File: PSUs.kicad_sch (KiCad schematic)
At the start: 57 parts, among them J6 Barrel_Jack, J7 AMP171826-4, Q1 DMP3013SFV-7, U3 AP64501SP-13, U4 AP64501SP-13, U8 AP62300WU-7

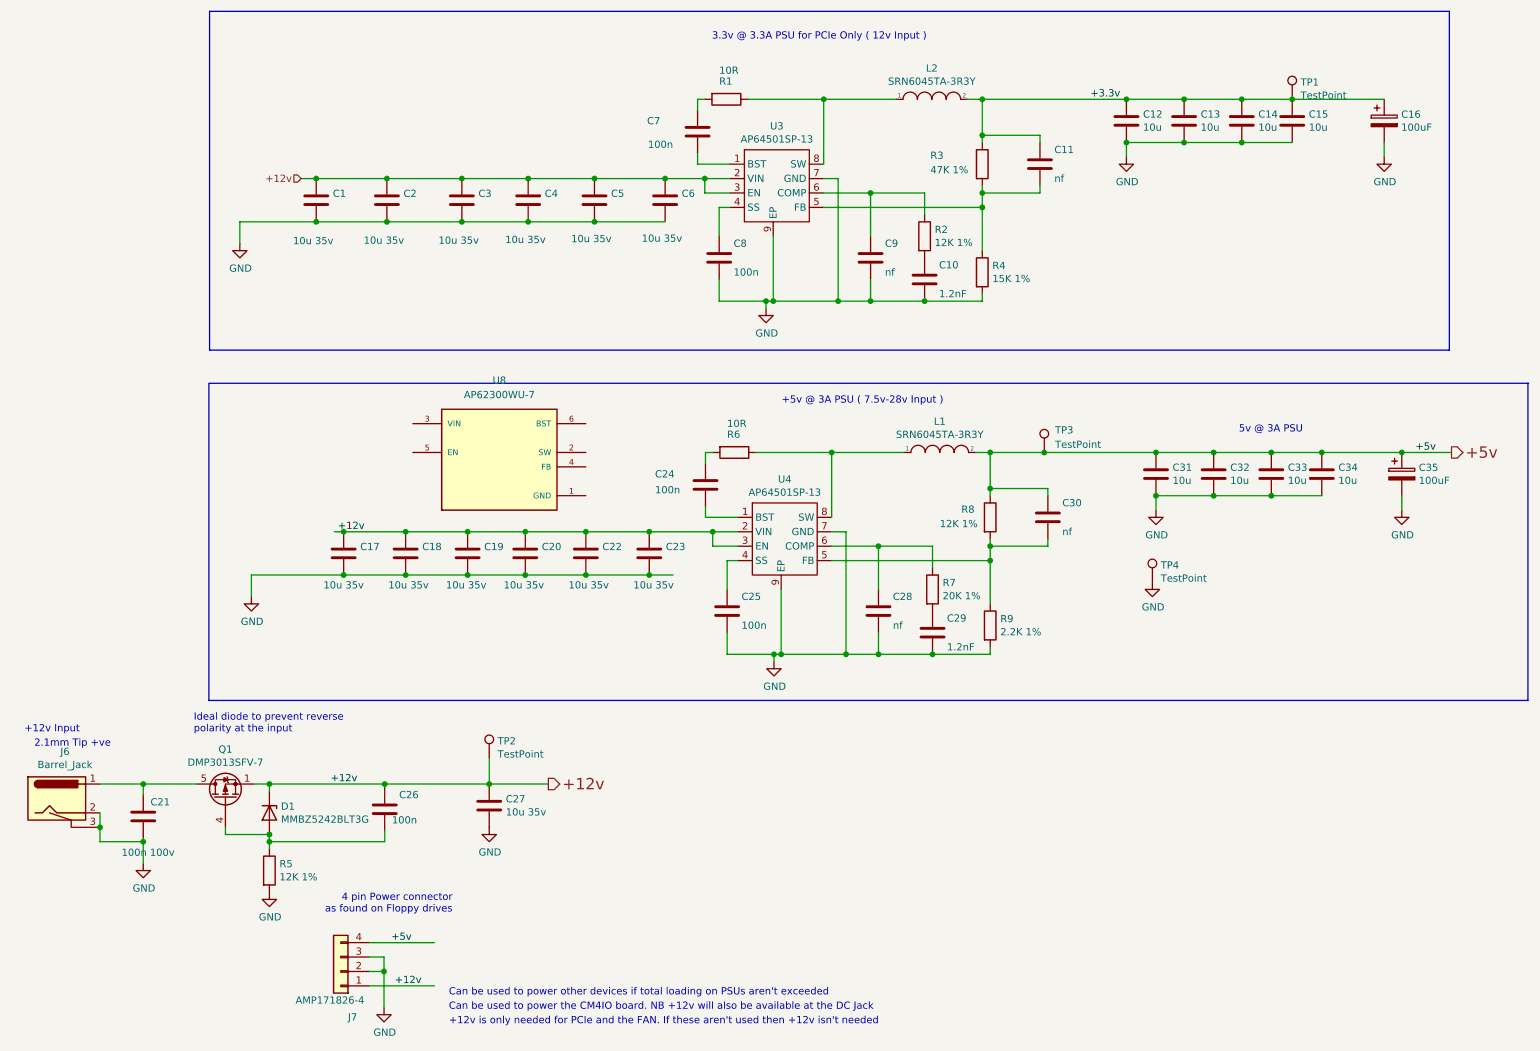
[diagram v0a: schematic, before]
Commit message: Added 3d-models, esd protection, cleaned up and made small start with pcb
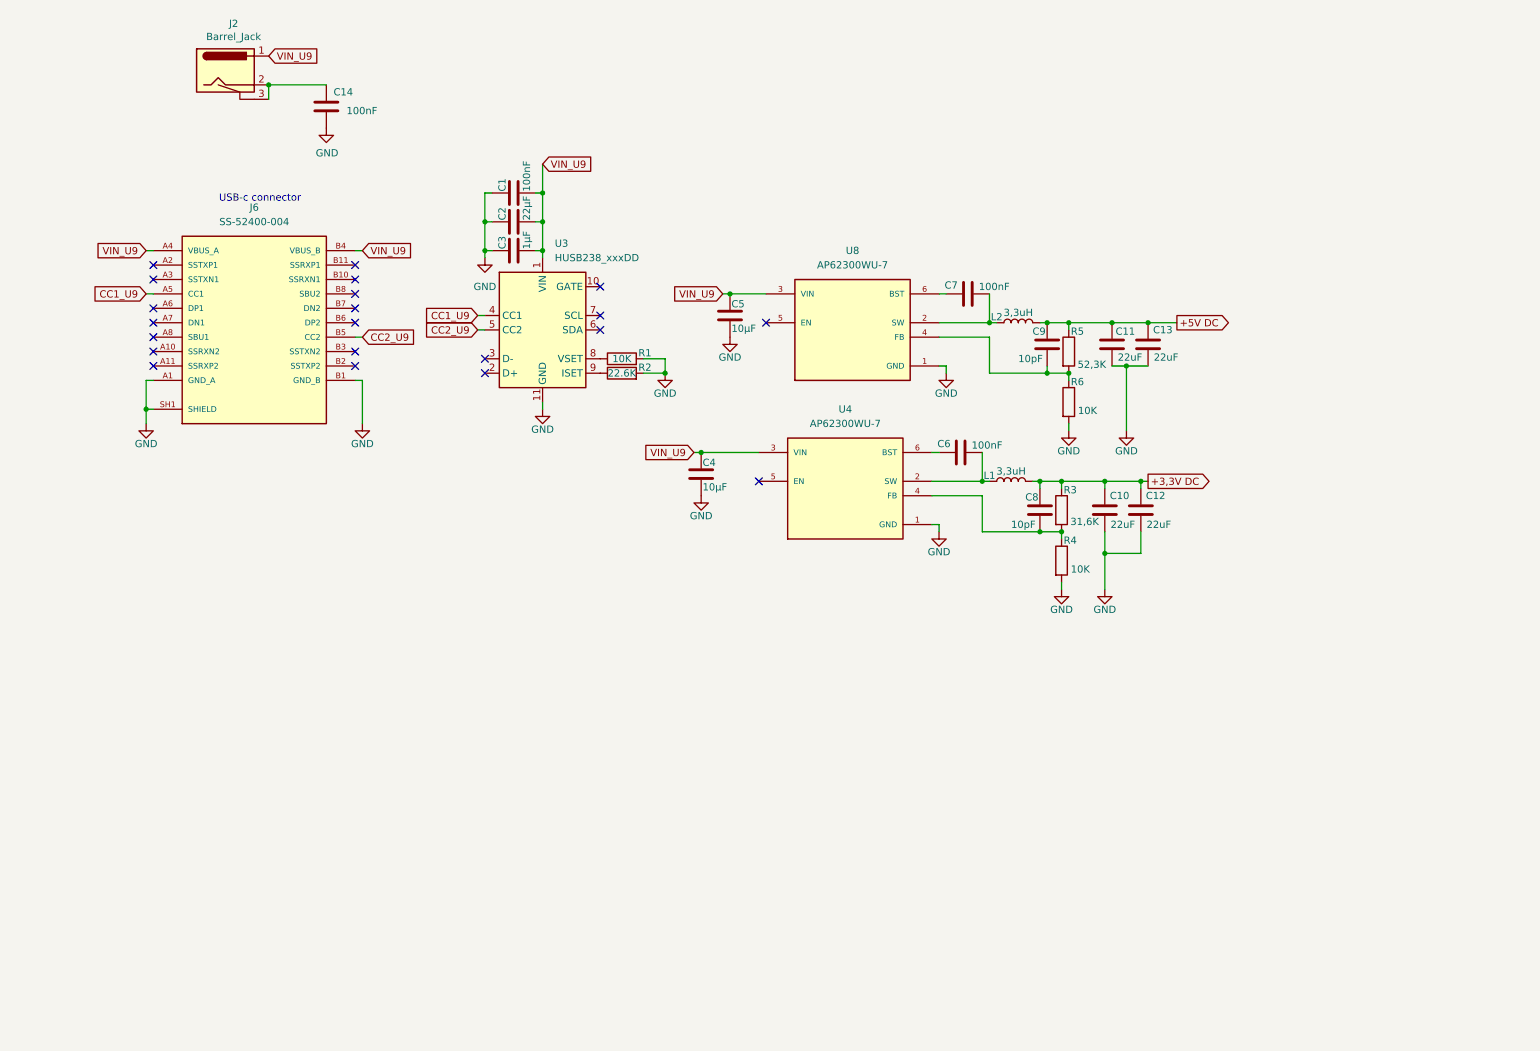
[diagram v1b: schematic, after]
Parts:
- removed C15, C31, C32, C33, C34: 10u, Capacitor_SMD:C_0805_2012Metric, symbol Device:C
- removed C16, C35: 100uF, Capacitor_Tantalum_SMD:CP_EIA-7343-31_Kemet-D, symbol Device:CP
- removed C17, C18, C19, C20, C22, C23, C27: 10u 35v, Capacitor_SMD:C_0805_2012Metric, symbol Device:C
- removed C21: 100n 100v, Capacitor_SMD:C_0402_1005Metric, symbol Device:C
- removed C24, C25, C26: 100n, Capacitor_SMD:C_0402_1005Metric, symbol Device:C
- removed C28, C30: nf, Capacitor_SMD:C_0402_1005Metric, symbol Device:C
- removed C29: 1.2nF, Capacitor_SMD:C_0402_1005Metric, symbol Device:C
- removed D1: MMBZ5242BLT3G, Diode_SMD:D_SOT-23_ANK, symbol Diode:BZX84Cxx
- removed J6: Barrel_Jack, CM4IO:BarrelJack_Horizontal, symbol CM4IO:Barrel_Jack
- removed J7: AMP171826-4, 171826-4:TE_171826-4, symbol Connector_Generic:Conn_01x04
- removed L1, L2: SRN6045TA-3R3Y, Inductor_SMD:L_Bourns_SRN6045TA, symbol pspice:INDUCTOR
- removed Q1: DMP3013SFV-7, Package_SON:Diodes_PowerDI3333-8, symbol Transistor_FET:DMP3013SFV
- removed R7: 20K 1%, Resistor_SMD:R_0402_1005Metric, symbol Device:R
- removed R8: 12K 1%, Resistor_SMD:R_0402_1005Metric, symbol Device:R
- removed R9: 2.2K 1%, Resistor_SMD:R_0402_1005Metric, symbol Device:R
- removed TP1, TP2, TP3, TP4: TestPoint, TestPoint:TestPoint_Pad_2.0x2.0mm, symbol Connector:TestPoint
- removed U3: AP64501SP-13, CM4IO:SOIC-8-1EP_3.9x4.9mm_P1.27mm_EP2.95x4.9mm_Mask2.71x3.4mm_ThermalVias, symbol CM4IO:AP64351
- removed U4: AP64501SP-13, Package_SO:SOIC-8-1EP_3.9x4.9mm_P1.27mm_EP2.95x4.9mm_Mask2.71x3.4mm_ThermalVias, symbol CM4IO:AP64351
- added J2: Barrel_Jack, CM4IO:BarrelJack_Horizontal, symbol CM4IO:Barrel_Jack
- added J6: SS-52400-004, SS-52400-004 (USB-c connector):STEWART_SS-52400-004 (USB-C), symbol SS-52400-004:SS-52400-004
- added L1, L2: 3,3uH, Inductor_SMD:L_0603_1608Metric, symbol Device:L
- added U3: HUSB238_xxxDD, Package_DFN_QFN:WDFN-10-1EP_3x3mm_P0.5mm_EP1.8x2.5mm, symbol Interface_USB:HUSB238_xxxDD
- added U4: AP62300WU-7, AP62300WU-7:SOT95P280X100-6N, symbol AP62300WU-7:AP62300WU-7
- C1, C6: value 10u 35v -> 100nF; footprint Capacitor_SMD:C_0805_2012Metric -> Capacitor_SMD:C_0603_1608Metric; Field4 Digikey -> (none); Field5 490-10505-1-ND -> (none); Field6 GRM21BC8YA106KE11L -> (none); Field7 Murata -> (none); Part Description 10uF 10% or 20% 35V Ceramic Capacitor X6S 0805 (2012 Metric) -> (none)
- C10: value 1.2nF -> 22uF; footprint Capacitor_SMD:C_0402_1005Metric -> Capacitor_SMD:C_0603_1608Metric; Field4 Digikey -> (none); Field5 490-16429-1-ND -> (none); Field6 GCM155R71H122KA37D -> (none); Field7 Murata -> (none); Part Description 1200pF 10% 10V Ceramic Capacitor X5R 0402 (1005 Metric) -> (none)
- C11: value nf -> 22uF; footprint Capacitor_SMD:C_0402_1005Metric -> Capacitor_SMD:C_0603_1608Metric; Field4 Digikey -> (none); Field5 490-17672-2-ND -> (none); Field6 GJM1555C1H270JB01D -> (none); Field7 Murata -> (none); Part Description 27pF 5% 50V Ceramic Capacitor C0G, NP0 0402 (1005 Metric) -> (none)
- C12, C13: value 10u -> 22uF; footprint Capacitor_SMD:C_0805_2012Metric -> Capacitor_SMD:C_0603_1608Metric; Field4 Digikey -> (none); Field5 490-14381-1-ND -> (none); Field6 GRM21BR71A106KA73L -> (none); Field7 Murata -> (none); Field8 111893011 -> (none); Part Description 10uF 10% 10V Ceramic Capacitor X7R 0805 (2012 Metric) -> (none)
- C14: value 10u -> 100nF; footprint Capacitor_SMD:C_0805_2012Metric -> Capacitor_SMD:C_0603_1608Metric; Field4 Digikey -> Farnell; Field5 490-14381-1-ND -> 2611907; Field6 GRM21BR71A106KA73L -> GRM155R62A104KE14D; Field8 111893011 -> (none); Part Description 10uF 10% 10V Ceramic Capacitor X7R 0805 (2012 Metric) -> 0.1uF 10% 100V Ceramic Capacitor X5R 0402 (1005 Metric)
- C2: value 10u 35v -> 22µF; footprint Capacitor_SMD:C_0805_2012Metric -> Capacitor_SMD:C_0603_1608Metric; Field4 Digikey -> (none); Field5 490-10505-1-ND -> (none); Field6 GRM21BC8YA106KE11L -> (none); Field7 Murata -> (none); Part Description 10uF 10% or 20% 35V Ceramic Capacitor X6S 0805 (2012 Metric) -> (none)
- C3: value 10u 35v -> 1µF; footprint Capacitor_SMD:C_0805_2012Metric -> Capacitor_SMD:C_0603_1608Metric; Field4 Digikey -> (none); Field5 490-10505-1-ND -> (none); Field6 GRM21BC8YA106KE11L -> (none); Field7 Murata -> (none); Part Description 10uF 10% or 20% 35V Ceramic Capacitor X6S 0805 (2012 Metric) -> (none)
- C4, C5: value 10u 35v -> 10µF; footprint Capacitor_SMD:C_0805_2012Metric -> Capacitor_SMD:C_0603_1608Metric; Field4 Digikey -> (none); Field5 490-10505-1-ND -> (none); Field6 GRM21BC8YA106KE11L -> (none); Field7 Murata -> (none); Part Description 10uF 10% or 20% 35V Ceramic Capacitor X6S 0805 (2012 Metric) -> (none)
- C7: value 100n -> 100nF; footprint Capacitor_SMD:C_0402_1005Metric -> Capacitor_SMD:C_0603_1608Metric; Field4 Farnell -> (none); Field5 2611911 -> (none); Field6 RM EMK105 B7104KV-F -> (none); Field7 TAIYO YUDEN EUROPE GMBH -> (none); Field8 110091611 -> (none); Part Description 0.1uF 10% 16V Ceramic Capacitor X7R 0402 (1005 Metric) -> (none)
- C8: value 100n -> 10pF; footprint Capacitor_SMD:C_0402_1005Metric -> Capacitor_SMD:C_0603_1608Metric; Field4 Farnell -> (none); Field5 2611911 -> (none); Field6 RM EMK105 B7104KV-F -> (none); Field7 TAIYO YUDEN EUROPE GMBH -> (none); Field8 110091611 -> (none); Part Description 0.1uF 10% 16V Ceramic Capacitor X7R 0402 (1005 Metric) -> (none)
- C9: value nf -> 10pF; footprint Capacitor_SMD:C_0402_1005Metric -> Capacitor_SMD:C_0603_1608Metric
- R1, R6: value 10R -> 10K; footprint Resistor_SMD:R_0402_1005Metric -> Resistor_SMD:R_0603_1608Metric; Field4 Farnell -> (none); Field5 9238999 -> (none); Field6 RC0402FR-0710RL -> (none); Field7 Yageo -> (none); Field8 URES00256 -> (none); Part Description Resistor 10R M1005 1% 63mW -> (none)
- R2: value 12K 1% -> 22.6K; footprint Resistor_SMD:R_0402_1005Metric -> Resistor_SMD:R_0603_1608Metric; Field4 Farnell -> (none); Field5 9239367 -> (none); Field6 MCR01MZPF1202 -> (none); Field7 Rohm -> (none); Part Description Resistor 12K M1005 1% 63mW -> (none)
- R3: value 47K 1% -> 31,6K; footprint Resistor_SMD:R_0402_1005Metric -> Resistor_SMD:R_0603_1608Metric; Field4 Farnell -> (none); Field5 9239430 -> (none); Field6 RK73G1ETQTP4702D -> (none); Field7 KOA EUROPE GMBH -> (none); Field8 120892781 -> (none); Part Description Resistor 47K M1005 1% 63mW -> (none)
- R4: value 15K 1% -> 10K; footprint Resistor_SMD:R_0402_1005Metric -> Resistor_SMD:R_0603_1608Metric; Field4 Farnell -> (none); Field5 9239375 -> (none); Field6 MCR01MZPF1502 -> (none); Field7 Rohm -> (none); Field8 120891581 -> (none); Part Description Resistor 15K M1005 1% 63mW -> (none)
- R5: value 12K 1% -> 52,3K; footprint Resistor_SMD:R_0402_1005Metric -> Resistor_SMD:R_0603_1608Metric; Field4 Farnell -> (none); Field5 9239367 -> (none); Field6 MCR01MZPF1202 -> (none); Field7 Rohm -> (none); Part Description Resistor 12K M1005 1% 63mW -> (none)
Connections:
- net GND: now also C1.1, C10.1, C11.1, C12.1, C13.1, C2.1, C3.1, R1.2, R2.2, R6.2, U8.1 (GND), J6.A1 (GND_A), J6.A12 (GND_A), J6.B1 (GND_B), J6.B12 (GND_B), J6.SH1 (SHIELD), J6.SH2 (SHIELD), J6.SH3 (SHIELD), J6.SH4 (SHIELD), U3.11 (GND), U4.1 (GND); no longer C1.2, C10.2, C12.2, C13.2, C2.2, C3.2, C6.2, C8.2, C9.2, R5.2
- net at R1.1: now also U3.8 (VSET)
- net +5V DC: now reaches R5.1
- net +5V DC: now also C11.2, C13.2, C9.2, L2.2
- net at C9.1: now also R5.2, R6.1, U8.4 (FB); no longer R2.1
- net at R3.2, R4.1: now also C8.1, U4.4 (FB); no longer C11.2
- net at C7.2: now also U8.2 (SW), L2.1
- net at C7.1: now also U8.6 (BST); no longer R1.2
- net VBUS_A: now reaches U8.3 (VIN)
- net VBUS_A: now also C1.2, C2.2, C3.2, C4.1, C5.1, J2.1, J6.A4 (VBUS_A), J6.A9 (VBUS_A), J6.B4 (VBUS_B), J6.B9 (VBUS_B), U3.1 (VIN), U4.3 (VIN)
- removed net +12v: C1.1, C2.1, C3.1, C4.1, C5.1, C6.1
- removed net +3.3v: C11.1, C12.1, C13.1, C14.1, R3.1
- new net: C14.1, J2.2, J2.3
- new net: R2.1, U3.9 (ISET)
- new net: C6.1, U4.6 (BST)
- new net: C6.2, L1.1, U4.2 (SW)
- new net +3,3V DC: C10.2, C12.2, C8.2, L1.2, R3.1
- new net CC1_U9: J6.A5 (CC1), U3.4 (CC1)
- new net CC2_U9: J6.B5 (CC2), U3.5 (CC2)
- no-connect marks 0 -> 21
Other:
- note added: "USB-c connector"
- note removed: "+12v Input"
- note removed: "+12v is only needed for PCIe and the FAN. If these aren't used then +12v isn't needed"
- note removed: "+5v @ 3A PSU ( 7.5v-28v Input )"
- note removed: "2.1mm Tip +ve"
- note removed: "3.3v @ 3.3A PSU for PCIe Only ( 12v Input )"
- note removed: "4 pin Power connector as found on Floppy drives"
- note removed: "5v @ 3A PSU"
- note removed: "Can be used to power other devices if total loading on PSUs aren't exceeded"
- note removed: "Can be used to power the CM4IO board. NB +12v will also be available at the DC Jack"
- note removed: "Ideal diode to prevent reverse polarity at the input"
- moved on the sheet: U8

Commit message: Adjusted the PCB design, changed footprints to 0402 (temp)
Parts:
- C1, C10, C11, C12, C13, C14, C2, C3, C4, C5, C6, C7, C8, C9: footprint Capacitor_SMD:C_0603_1608Metric -> Capacitor_SMD:C_0402_1005Metric_Pad0.74x0.62mm_HandSolder
- R1, R2, R3, R4, R5, R6: footprint Resistor_SMD:R_0603_1608Metric -> Resistor_SMD:R_0402_1005Metric_Pad0.72x0.64mm_HandSolder
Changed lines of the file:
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@@
 			)
 		)
-		(property "Footprint" "Capacitor_SMD:C_0603_1608Metric"
+		(property "Footprint" "Capacitor_SMD:C_0402_1005Metric_Pad0.74x0.62mm_HandSolder"
 			(at 68.2752 38.1 0)
 			(effects
@@
 			)
 		)
-		(property "Footprint" "Resistor_SMD:R_0603_1608Metric"
+		(property "Footprint" "Resistor_SMD:R_0402_1005Metric_Pad0.72x0.64mm_HandSolder"
 			(at 196.342 86.36 90)
 			(effects
@@
 			)
 		)
-		(property "Footprint" "Capacitor_SMD:C_0603_1608Metric"
+		(property "Footprint" "Capacitor_SMD:C_0402_1005Metric_Pad0.74x0.62mm_HandSolder"
 			(at 193.3448 72.39 0)
 			(effects
@@
 			)
 		)
-		(property "Footprint" "Capacitor_SMD:C_0603_1608Metric"
+		(property "Footprint" "Capacitor_SMD:C_0402_1005Metric_Pad0.74x0.62mm_HandSolder"
 			(at 184.15 66.3448 0)
 			(effects
@@
 			)
 		)
-		(property "Footprint" "Resistor_SMD:R_0603_1608Metric"
+		(property "Footprint" "Resistor_SMD:R_0402_1005Metric_Pad0.72x0.64mm_HandSolder"
 			(at 119.38 83.058 90)
 			(effects
@@
 			)
 		)
-		(property "Footprint" "Capacitor_SMD:C_0603_1608Metric"
+		(property "Footprint" "Capacitor_SMD:C_0402_1005Metric_Pad0.74x0.62mm_HandSolder"
 			(at 182.88 94.2848 0)
 			(effects
@@
 			)
 		)
-		(property "Footprint" "Capacitor_SMD:C_0603_1608Metric"
+		(property "Footprint" "Capacitor_SMD:C_0402_1005Metric_Pad0.74x0.62mm_HandSolder"
 			(at 204.7748 72.39 0)
 			(effects
@@
 			)
 		)
-		(property "Footprint" "Resistor_SMD:R_0603_1608Metric"
+		(property "Footprint" "Resistor_SMD:R_0402_1005Metric_Pad0.72x0.64mm_HandSolder"
 			(at 195.072 114.3 90)
 			(effects
@@
 			)
 		)
-		(property "Footprint" "Capacitor_SMD:C_0603_1608Metric"
+		(property "Footprint" "Capacitor_SMD:C_0402_1005Metric_Pad0.74x0.62mm_HandSolder"
 			(at 139.3952 74.93 0)
 			(effects
@@
 			)
 		)
-		(property "Footprint" "Capacitor_SMD:C_0603_1608Metric"
+		(property "Footprint" "Capacitor_SMD:C_0402_1005Metric_Pad0.74x0.62mm_HandSolder"
 			(at 104.14 53.6448 0)
 			(effects
@@
 			)
 		)
-		(property "Footprint" "Resistor_SMD:R_0603_1608Metric"
+		(property "Footprint" "Resistor_SMD:R_0402_1005Metric_Pad0.72x0.64mm_HandSolder"
 			(at 196.342 77.47 90)
 			(effects
@@
 			)
 		)
-		(property "Footprint" "Capacitor_SMD:C_0603_1608Metric"
+		(property "Footprint" "Capacitor_SMD:C_0402_1005Metric_Pad0.74x0.62mm_HandSolder"
 			(at 211.1248 72.39 0)
 			(effects
@@
 			)
 		)
-		(property "Footprint" "Capacitor_SMD:C_0603_1608Metric"
+		(property "Footprint" "Capacitor_SMD:C_0402_1005Metric_Pad0.74x0.62mm_HandSolder"
 			(at 104.14 48.5648 0)
 			(effects
@@
 			)
 		)
-		(property "Footprint" "Capacitor_SMD:C_0603_1608Metric"
+		(property "Footprint" "Capacitor_SMD:C_0402_1005Metric_Pad0.74x0.62mm_HandSolder"
 			(at 203.5048 101.6 0)
 			(effects
@@
 			)
 		)
-		(property "Footprint" "Capacitor_SMD:C_0603_1608Metric"
+		(property "Footprint" "Capacitor_SMD:C_0402_1005Metric_Pad0.74x0.62mm_HandSolder"
 			(at 192.0748 101.6 0)
 			(effects
@@
 			)
 		)
-		(property "Footprint" "Capacitor_SMD:C_0603_1608Metric"
+		(property "Footprint" "Capacitor_SMD:C_0402_1005Metric_Pad0.74x0.62mm_HandSolder"
 			(at 104.14 58.7248 0)
 			(effects
@@
 			)
 		)
-		(property "Footprint" "Capacitor_SMD:C_0603_1608Metric"
+		(property "Footprint" "Capacitor_SMD:C_0402_1005Metric_Pad0.74x0.62mm_HandSolder"
 			(at 134.3152 102.87 0)
 			(effects
@@
 			)
 		)
-		(property "Footprint" "Resistor_SMD:R_0603_1608Metric"
+		(property "Footprint" "Resistor_SMD:R_0402_1005Metric_Pad0.72x0.64mm_HandSolder"
 			(at 119.38 80.518 90)
 			(effects
@@
 			)
 		)
-		(property "Footprint" "Capacitor_SMD:C_0603_1608Metric"
+		(property "Footprint" "Capacitor_SMD:C_0402_1005Metric_Pad0.74x0.62mm_HandSolder"
 			(at 209.8548 101.6 0)
 			(effects
@@
 			)
 		)
-		(property "Footprint" "Resistor_SMD:R_0603_1608Metric"
+		(property "Footprint" "Resistor_SMD:R_0402_1005Metric_Pad0.72x0.64mm_HandSolder"
 			(at 195.072 105.41 90)
 			(effects
